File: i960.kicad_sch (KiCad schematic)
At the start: 46 parts

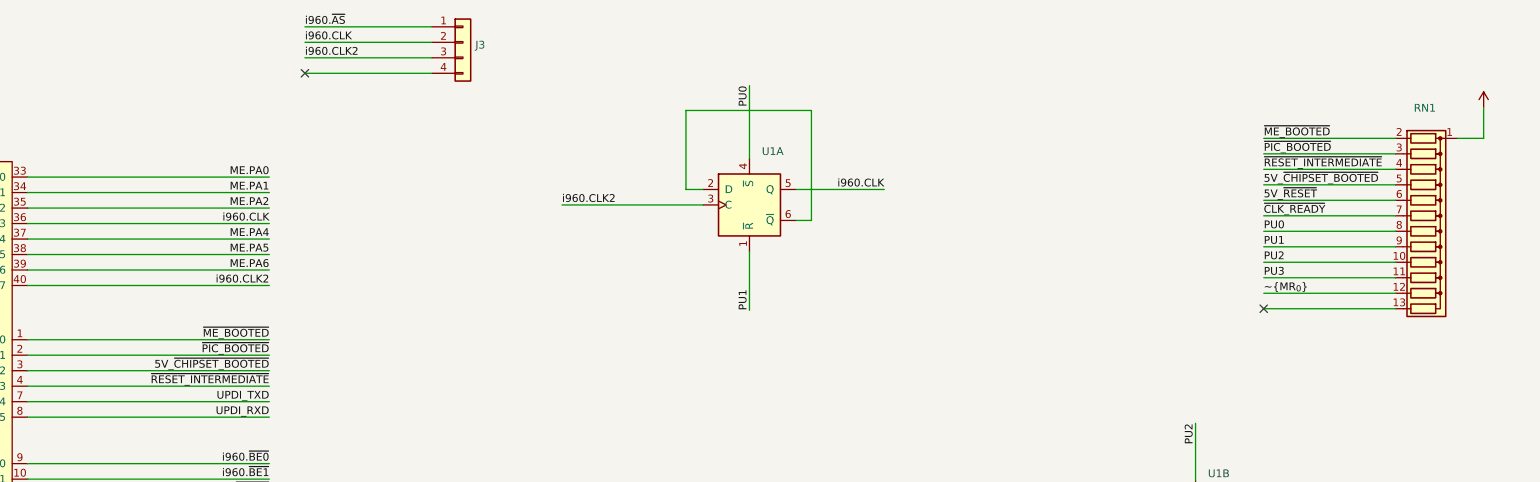
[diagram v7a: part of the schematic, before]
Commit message: Get rid of ME_BOOTED because it is no longer necessary with the reset circuit no longer handled by a CCL.
Turns out to be a massive waste that way otherwise.
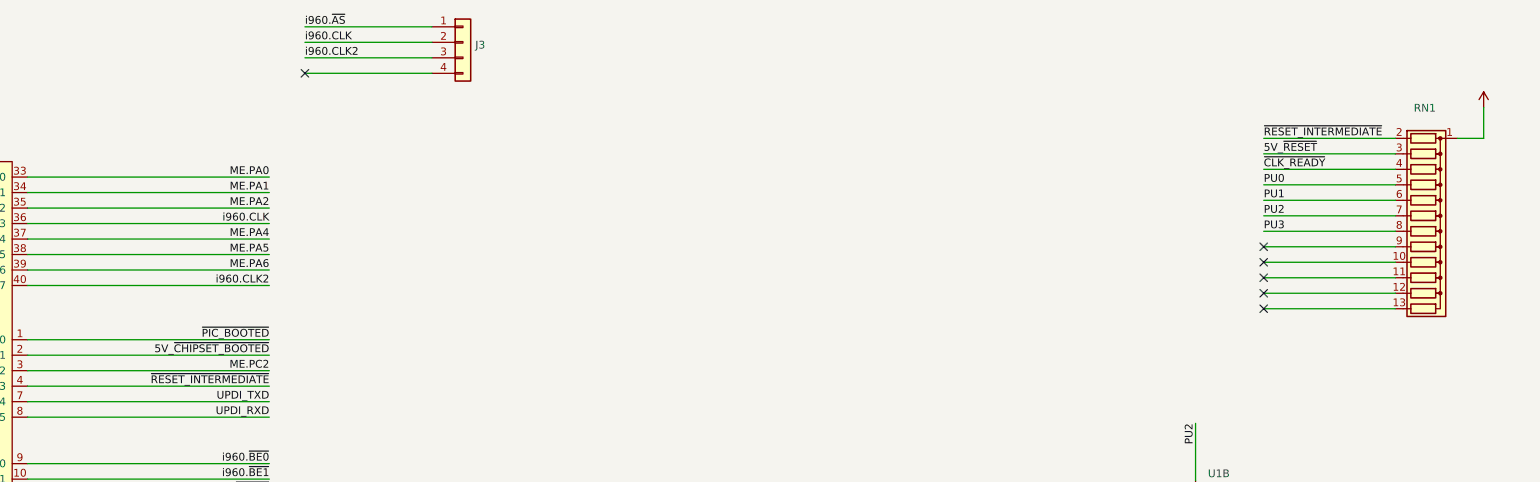
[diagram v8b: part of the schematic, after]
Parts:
- removed unit 1 of U1
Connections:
- net 5V_~{CHIPSET_BOOTED}: now also U16.2 ((RXD1/MISO_ALT/CCL1-IN1)PC1); no longer RN1.5 (R4), U16.3 ((XCK1/SCK_ALT/CCL1-IN2)PC2)
- net 5V_~{RESET}: now also RN1.3 (R2); no longer RN1.6 (R5)
- net PU0: now also RN1.5 (R4); no longer RN1.8 (R7)
- net PU1: now also RN1.6 (R5); no longer RN1.9 (R8)
- net PU2: now also RN1.7 (R6); no longer RN1.10 (R9)
- net PU3: now also RN1.8 (R7); no longer RN1.11 (R10)
- net ~{CLK_READY}: now also RN1.4 (R3); no longer RN1.7 (R6)
- net ~{PIC_BOOTED}: now also U16.1 ((TXD1/MOSI_ALT/CCL1-IN0)PC0); no longer RN1.3 (R2), U16.2 ((RXD1/MISO_ALT/CCL1-IN1)PC1)
- net ~{RESET_INTERMEDIATE}: now also RN1.2 (R1); no longer RN1.4 (R3)
- removed net ~{ME_BOOTED}: RN1.2 (R1), U16.1 ((TXD1/MOSI_ALT/CCL1-IN0)PC0)
- net ~{MR_{0}}: no longer names the net of RN1.12 (R11)
- new net ME.PC2: U16.3 ((XCK1/SCK_ALT/CCL1-IN2)PC2)
- no-connect marks 13 -> 17
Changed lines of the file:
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@@
   (no_connect (at 263.398 455.168))
   (no_connect (at 263.398 457.708))
+  (no_connect (at 305.562 53.848))
+  (no_connect (at 305.562 56.388))
+  (no_connect (at 305.562 58.928))
   (no_connect (at 285.496 549.91))
   (no_connect (at 367.284 549.91))
+  (no_connect (at 305.562 61.468))
   (no_connect (at 24.13 346.71))
   (no_connect (at 305.562 64.008))
@@
     (stroke (width 0) (type default) (color 0 0 0 0))
   )
-  (wire (pts (xy 221.234 27.432) (xy 221.234 39.37))
-    (stroke (width 0) (type default) (color 0 0 0 0))
-  )
   (wire (pts (xy 442.976 129.794) (xy 470.662 129.794))
     (stroke (width 0) (type default) (color 0 0 0 0))
@@
     (stroke (width 0) (type default) (color 0 0 0 0))
   )
-  (wire (pts (xy 221.234 54.61) (xy 221.234 64.262))
-    (stroke (width 0) (type default) (color 0 0 0 0))
-  )
   (wire (pts (xy 358.14 365.252) (xy 358.14 372.872))
     (stroke (width 0) (type default) (color 0 0 0 0))
@@
     (stroke (width 0) (type default) (color 0 0 0 0))
   )
-  (wire (pts (xy 231.394 49.53) (xy 231.394 31.496))
-    (stroke (width 0) (type default) (color 0 0 0 0))
-  )
   (wire (pts (xy 150.114 216.408) (xy 189.738 216.408))
     (stroke (width 0) (type default) (color 0 0 0 0))
@@
     (stroke (width 0) (type default) (color 0 0 0 0))
   )
-  (wire (pts (xy 228.854 44.45) (xy 243.332 44.45))
-    (stroke (width 0) (type default) (color 0 0 0 0))
-  )
   (bus (pts (xy 473.202 124.714) (xy 473.202 127.254))
     (stroke (width 0) (type default) (color 0 0 0 0))
@@
     (stroke (width 0) (type default) (color 0 0 0 0))
   )
-  (wire (pts (xy 190.5 46.99) (xy 213.614 46.99))
-    (stroke (width 0) (type default) (color 0 0 0 0))
-  )
   (wire (pts (xy 337.312 36.068) (xy 341.63 36.068))
     (stroke (width 0) (type default) (color 0 0 0 0))
@@
     (stroke (width 0) (type default) (color 0 0 0 0))
   )
-  (wire (pts (xy 228.854 49.53) (xy 231.394 49.53))
-    (stroke (width 0) (type default) (color 0 0 0 0))
-  )
   (wire (pts (xy 163.576 507.492) (xy 154.94 507.492))
     (stroke (width 0) (type default) (color 0 0 0 0))
@@
     (stroke (width 0) (type default) (color 0 0 0 0))
   )
-  (wire (pts (xy 231.394 31.496) (xy 210.82 31.496))
-    (stroke (width 0) (type default) (color 0 0 0 0))
-  )
   (wire (pts (xy 150.114 226.568) (xy 189.738 226.568))
     (stroke (width 0) (type default) (color 0 0 0 0))
@@
     (stroke (width 0) (type default) (color 0 0 0 0))
   )
-  (wire (pts (xy 210.82 44.45) (xy 213.614 44.45))
-    (stroke (width 0) (type default) (color 0 0 0 0))
-  )
   (wire (pts (xy 190.754 452.628) (xy 214.376 452.628))
     (stroke (width 0) (type default) (color 0 0 0 0))
@@
     (stroke (width 0) (type default) (color 0 0 0 0))
   )
-  (wire (pts (xy 210.82 31.496) (xy 210.82 44.45))
-    (stroke (width 0) (type default) (color 0 0 0 0))
-  )
   (wire (pts (xy 391.16 100.076) (xy 391.16 92.202))
     (stroke (width 0) (type default) (color 0 0 0 0))
@@
     (effects (font (size 1.27 1.27)) (justify left bottom))
   )
-  (label "PU0" (at 305.562 51.308 0)
+  (label "PU0" (at 305.562 43.688 0)
     (effects (font (size 1.27 1.27)) (justify left bottom))
   )
@@
     (effects (font (size 1.27 1.27)) (justify left bottom))
   )
-  (label "~{ME_BOOTED}" (at 305.562 36.068 0)
-    (effects (font (size 1.27 1.27)) (justify left bottom))
-  )
   (label "~{PIC_BOOTED}" (at 189.738 304.038 180)
     (effects (font (size 1.27 1.27)) (justify right bottom))
@@
     (effects (font (size 1.27 1.27)) (justify left bottom))
   )
-  (label "i960.CLK2" (at 190.5 46.99 0)
-    (effects (font (size 1.27 1.27)) (justify left bottom))
-  )
   (label "ME.PA2" (at 142.494 47.498 180)
     (effects (font (size 1.27 1.27)) (justify right bottom))
@@
     (effects (font (size 1.27 1.27)) (justify right bottom))
   )
-  (label "5V_~{CHIPSET_BOOTED}" (at 305.562 43.688 0)
-    (effects (font (size 1.27 1.27)) (justify left bottom))
-  )
   (label "i960.~{BE0}" (at 570.738 186.182 180)
     (effects (font (size 1.27 1.27)) (justify right bottom))
@@
     (effects (font (size 1.27 1.27)) (justify right bottom))
   )
+  (label "ME.PC2" (at 142.494 74.168 180)
+    (effects (font (size 1.27 1.27)) (justify right bottom))
+  )
   (label "PIC.RX" (at 189.738 221.488 180)
     (effects (font (size 1.27 1.27)) (justify right bottom))
@@
     (effects (font (size 1.27 1.27)) (justify left bottom))
   )
-  (label "PU3" (at 305.562 58.928 0)
+  (label "PU3" (at 305.562 51.308 0)
     (effects (font (size 1.27 1.27)) (justify left bottom))
   )
@@
     (effects (font (size 1.27 1.27)) (justify left bottom))
   )
-  (label "~{ME_BOOTED}" (at 142.494 69.088 180)
-    (effects (font (size 1.27 1.27)) (justify right bottom))
-  )
   (label "INT3_OUT" (at 341.122 385.572 0)
     (effects (font (size 1.27 1.27)) (justify left bottom))
@@
     (effects (font (size 1.27 1.27)) (justify right bottom))
   )
-  (label "~{RESET_INTERMEDIATE}" (at 305.562 41.148 0)
+  (label "~{RESET_INTERMEDIATE}" (at 305.562 36.068 0)
     (effects (font (size 1.27 1.27)) (justify left bottom))
   )
@@
     (effects (font (size 1.27 1.27)) (justify right bottom))
   )
-  (label "PU0" (at 221.234 27.432 270)
-    (effects (font (size 1.27 1.27)) (justify right bottom))
-  )
   (label "UPDI2" (at 67.31 227.838 0)
     (effects (font (size 1.27 1.27)) (justify left bottom))
@@
     (effects (font (size 1.27 1.27)) (justify right bottom))
   )
-  (label "i960.CLK" (at 243.332 44.45 180)
-    (effects (font (size 1.27 1.27)) (justify right bottom))
-  )
   (label "i960.A21" (at 493.522 278.384 0)
     (effects (font (size 1.27 1.27)) (justify left bottom))
@@
     (effects (font (size 1.27 1.27)) (justify left bottom))
   )
-  (label "~{PIC_BOOTED}" (at 142.494 71.628 180)
+  (label "~{PIC_BOOTED}" (at 142.494 69.088 180)
     (effects (font (size 1.27 1.27)) (justify right bottom))
   )
@@
     (effects (font (size 1.27 1.27)) (justify right bottom))
   )
-  (label "PU2" (at 305.562 56.388 0)
+  (label "PU2" (at 305.562 48.768 0)
     (effects (font (size 1.27 1.27)) (justify left bottom))
   )
@@
     (effects (font (size 1.27 1.27)) (justify left bottom))
   )
-  (label "~{MR_{0}}" (at 305.562 61.468 0)
-    (effects (font (size 1.27 1.27)) (justify left bottom))
-  )
   (label "AD11" (at 380.492 181.356 0)
     (effects (font (size 1.27 1.27)) (justify left bottom))
@@
     (effects (font (size 1.27 1.27)) (justify left bottom))
   )
-  (label "PU1" (at 305.562 53.848 0)
+  (label "PU1" (at 305.562 46.228 0)
     (effects (font (size 1.27 1.27)) (justify left bottom))
   )
@@
     (effects (font (size 1.27 1.27)) (justify left bottom))
   )
-  (label "~{PIC_BOOTED}" (at 305.562 38.608 0)
-    (effects (font (size 1.27 1.27)) (justify left bottom))
-  )
   (label "UPDI_RXD2" (at 189.738 248.158 180)
     (effects (font (size 1.27 1.27)) (justify right bottom))
@@
     (effects (font (size 1.27 1.27)) (justify left bottom))
   )
-  (label "PU1" (at 221.234 64.262 90)
-    (effects (font (size 1.27 1.27)) (justify left bottom))
-  )
   (label "PIC.PE3" (at 189.738 286.258 180)
     (effects (font (size 1.27 1.27)) (justify right bottom))
@@
     (effects (font (size 1.27 1.27)) (justify left bottom))
   )
-  (label "~{CLK_READY}" (at 305.562 48.768 0)
+  (label "~{CLK_READY}" (at 305.562 41.148 0)
     (effects (font (size 1.27 1.27)) (justify left bottom))
   )
@@
     (effects (font (size 1.27 1.27)) (justify right bottom))
   )
-  (label "5V_~{RESET}" (at 305.562 46.228 0)
+  (label "5V_~{RESET}" (at 305.562 38.608 0)
     (effects (font (size 1.27 1.27)) (justify left bottom))
   )
@@
     (effects (font (size 1.27 1.27)) (justify left bottom))
   )
-  (label "5V_~{CHIPSET_BOOTED}" (at 142.494 74.168 180)
+  (label "5V_~{CHIPSET_BOOTED}" (at 142.494 71.628 180)
     (effects (font (size 1.27 1.27)) (justify right bottom))
   )
@@
     (pin "2")
   )
-  (symbol (lib_id "74xx:74LS74") (at 221.234 46.99 0) (unit 1)
-    (in_bom yes) (on_board yes) (fields_autoplaced)
-    (property "Reference" "U1" (id 0) (at 223.2534 38.2102 0)
-      (effects (font (size 1.27 1.27)) (justify left))
-    )
-    (property "Value" "" (id 1) (at 223.2534 40.7471 0)
-      (effects (font (size 1.27 1.27)) (justify left))
-    )
-    (property "Footprint" "" (id 2) (at 221.234 46.99 0)
-      (effects (font (size 1.27 1.27)) hide)
-    )
-    (property "Datasheet" "74xx/74hc_hct74.pdf" (id 3) (at 221.234 46.99 0)
-      (effects (font (size 1.27 1.27)) hide)
-    )
-    (pin "1")
-    (pin "2")
-    (pin "3")
-    (pin "4")
-    (pin "5")
-    (pin "6")
-    (pin "10")
-    (pin "11")
-    (pin "12")
-    (pin "13")
-    (pin "8")
-    (pin "9")
-    (pin "14")
-    (pin "7")
-  )
   (symbol (lib_id "power:+5V") (at 87.884 200.914 0) (unit 1)
